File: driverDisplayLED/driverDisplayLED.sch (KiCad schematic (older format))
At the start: 16 parts

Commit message: set: 74HC245D - CONN2X8 - 74HC245D - 74HC138D
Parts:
- added C?: C, symbol Device:C
- Q? (x2): symbol FDS4953:FDS4953 -> driverDisplayLED-rescue:FDS4953-FDS4953
- U?: symbol 74HC138D:74HC138D -> driverDisplayLED-rescue:74HC138D-74HC138D
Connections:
- net labels added: A6-A7, A7-B4, B0-b5, B1-a5, B2-b6, B3-a6, B4-E3, B4-b7, B5-E2, B5B6B7-b8, B6-B6, B7-B7, GND, VCC, a4-A5
- net labels removed: a4
- wire segments 14 -> 71
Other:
- moved on the sheet: U?

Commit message: primer bloque 74HC595D: shift-register
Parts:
- added C? (x3): C, symbol Device:C
- added J? (x2): Conn_01x12_Male, symbol Connector:Conn_01x12_Male
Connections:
- net labels added: A1-SER, A5-SRCLK, G1, G2, G3, G4, G5, G6, G7, G8, H5, H6, H7, H8, R1, R2, R3, R4, R5, R6, R7, R8, RCLK, SRCLK, bus.R8-R1
- wire segments 71 -> 129
- no-connect marks 0 -> 3
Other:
- moved on the sheet: C?, U?, U?A, U?B, U?C, U?D, U?E, U?F, U?G

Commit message: segundo bloque 74HC595D: shift-register
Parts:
- removed U?: 74HC595, symbol 74xx:74HC595
- added C? (x2): C, symbol Device:C
- added J? (x2): Conn_01x12_Male, symbol Connector:Conn_01x12_Male
- added U? (x2): 74HC595, symbol 74xx:74HC595
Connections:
- net labels added: QH-SER
- wire segments 129 -> 209

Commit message: bloque inverters, bloque mosfets. Pendiente: añadir segunda hoja a derecha, conectar matrices, completar 74HC245D(1), revisar los NC.
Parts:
- removed Q? (x2): FDS4953, SOIC127P600X175-8N, symbol driverDisplayLED-rescue:FDS4953-FDS4953
- removed U?: 74HC595, symbol 74xx:74HC595
- added C? (x3): C, symbol Device:C
- added D? (x2): D, symbol Device:D
- added J? (x4): Conn_01x12_Male, symbol Connector:Conn_01x12_Male
- added Q1, Q2, Q? (x6): FDS4953-FDS4953, SOIC127P600X175-8N, symbol driverDisplayLED-rescue:FDS4953-FDS4953
- added R? (x3): R, symbol Device:R
- added RN?: R_Network04, Resistor_THT:R_Array_SIP5, symbol Device:R_Network04
- added U?: 74HC595, symbol 74xx:74HC595
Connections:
- net labels added: 1, 2, 3, 4, 5, 6, 7, 8, Y0-G2, Y1-G1, Y2-G2, Y3-G1, bus.Y4-Y7
- wire segments 209 -> 402
- no-connect marks 3 -> 7
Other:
- moved on the sheet: C?, J?, U?, U?A, U?B, U?C, U?D, U?E, U?F, U?G

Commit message: netlist, asociación de componentes
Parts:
- C1, C2, C3, C4, C5, C6, C7, C8, C9: renamed from C?; footprint (none) -> Capacitor_SMD:CP_Elec_3x5.3
- D1, D2: renamed from D?; footprint (none) -> Diode_SMD:D_0201_0603Metric
- J1, J2, J3, J5, J6, J7, J8, J9: renamed from J?; footprint (none) -> Connector_PinHeader_1.00mm:PinHeader_1x12_P1.00mm_Vertical
- J4: renamed from J?; footprint (none) -> Connector_IDC:IDC-Header_2x08_P2.54mm_Vertical
- Q1, Q2: footprint SOIC127P600X175-8N -> FDS4953:SOIC127P600X175-8N
- Q1, Q2, Q3, Q4: renamed from Q?; footprint SOIC127P600X175-8N -> FDS4953:SOIC127P600X175-8N
- R1, R2, R3: renamed from R?; footprint (none) -> Resistor_SMD:R_0201_0603Metric
- RN1: renamed from RN?; footprint Resistor_THT:R_Array_SIP5 -> Resistor_THT:R_Array_SIP4
- U1, U4: renamed from U?; footprint (none) -> Package_SO:HSOP-20-1EP_11.0x15.9mm_P1.27mm_SlugDown_ThermalVias
- U2, U3, U7, U8: renamed from U?; footprint (none) -> Package_SO:HTSSOP-16-1EP_4.4x5mm_P0.65mm_EP3.4x5mm
- U5: renamed from U?; footprint SOIC127P600X175-16N -> Package_SO:TSSOP-16_4.4x5mm_P0.65mm
- U6: renamed from U?; footprint (none) -> Package_SO:TSSOP-14_4.4x5mm_P0.65mm
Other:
- moved on the sheet: C1, C3, C5, C6, C7, C8, C9, D1, D2, J3, J7, J8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

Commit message: cambio conector 2x08 J4
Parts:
- removed J4: Conn_02x08_Row_Letter_First, Connector_IDC:IDC-Header_2x08_P2.54mm_Vertical, symbol Connector_Generic:Conn_02x08_Row_Letter_First
- added J4: Conn_02x08_Counter_Clockwise, Connector_PinHeader_2.54mm:PinHeader_2x08_P2.54mm_Vertical, symbol Connector_Generic:Conn_02x08_Counter_Clockwise
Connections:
- wire segments 402 -> 399
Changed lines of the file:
@@
 	-6650 5550 -6550 5650
-$Comp
-L Connector_Generic:Conn_02x08_Row_Letter_First J4
-U 1 1 5F69521F
-P 3750 8150
-F 0 "J4" H 3800 8667 50  0000 C CNN
-F 1 "Conn_02x08_Row_Letter_First" H 3800 8576 50  0000 C CNN
-F 2 "Connector_IDC:IDC-Header_2x08_P2.54mm_Vertical" H 3750 8150 50  0001 C CNN
-F 3 "~" H 3750 8150 50  0001 C CNN
-	1    3750 8150
-	1    0    0    -1
-$EndComp
 $Comp
 L Device:C C3
@@
 Text Label 3100 7800 2    50   ~ 0
 B2-b6
-Wire Wire Line
-	3700 8350 3650 8350
 Text Label 3100 7900 2    50   ~ 0
 B3-a6
@@
 Text Label 4050 8900 2    50   ~ 0
 B2-b6
-Wire Wire Line
-	3650 8150 3700 8150
-Wire Wire Line
-	3650 8250 3700 8250
 Wire Wire Line
 	5850 8450 6000 8450
@@
 Wire Wire Line
 	700  1300 700  8100
+$Comp
+L Connector_Generic:Conn_02x08_Counter_Clockwise J4
+U 1 1 5F72EC68
+P 3750 8150
+F 0 "J4" H 3800 8667 50  0000 C CNN
+F 1 "Conn_02x08_Counter_Clockwise" H 3800 8576 50  0000 C CNN
+F 2 "Connector_PinHeader_2.54mm:PinHeader_2x08_P2.54mm_Vertical" H 3750 8150 50  0001 C CNN
+F 3 "~" H 3750 8150 50  0001 C CNN
+	1    3750 8150
+	1    0    0    -1
+$EndComp
 $EndSCHEMATC

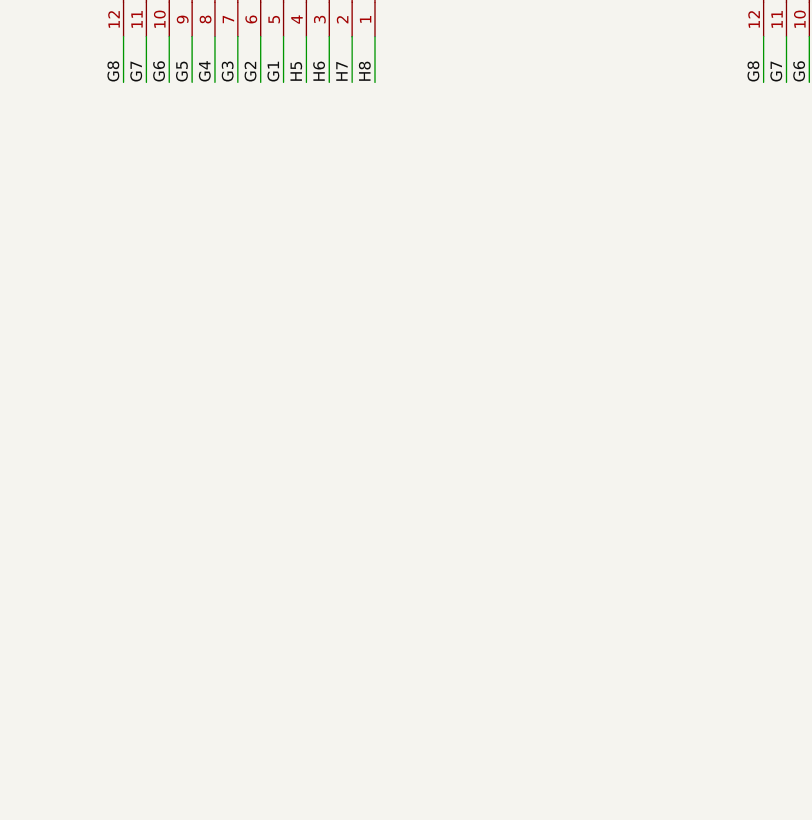
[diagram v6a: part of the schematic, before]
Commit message: agrego modulo myLedMatrix. Probar instanciar debido al path local
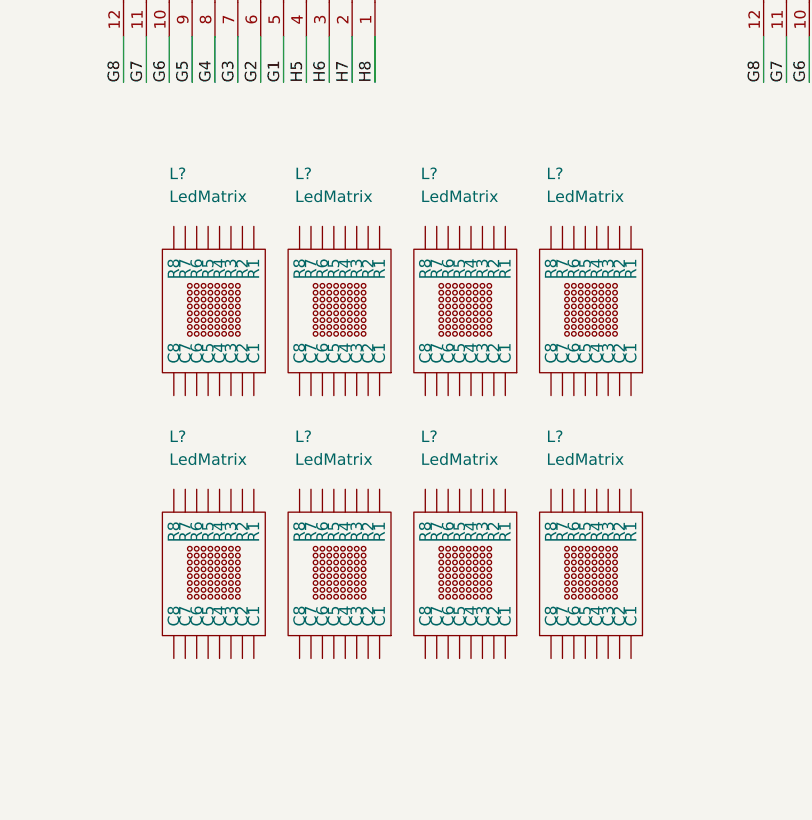
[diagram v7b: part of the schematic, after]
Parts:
- added L? (x8): LedMatrix, symbol myLedMatrix:LedMatrix
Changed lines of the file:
@@
 	1    0    0    -1
 $EndComp
+$Comp
+L myLedMatrix:LedMatrix L?
+U 1 1 5F7B4D9C
+P 1950 4550
+F 0 "L?" H 2150 3950 50  0000 R CNN
+F 1 "LedMatrix" H 2150 4050 50  0000 R CNN
+F 2 "" H 1930 4530 50  0001 C CNN
+F 3 "" H 1930 4530 50  0001 C CNN
+	1    1950 4550
+	-1   0    0    1
+$EndComp
+$Comp
+L myLedMatrix:LedMatrix L?
+U 1 1 5F7C4F20
+P 2500 4550
+F 0 "L?" H 2700 3950 50  0000 R CNN
+F 1 "LedMatrix" H 2700 4050 50  0000 R CNN
+F 2 "" H 2480 4530 50  0001 C CNN
+F 3 "" H 2480 4530 50  0001 C CNN
+	1    2500 4550
+	-1   0    0    1
+$EndComp
+$Comp
+L myLedMatrix:LedMatrix L?
+U 1 1 5F7C5FCF
+P 3050 4550
+F 0 "L?" H 3250 3950 50  0000 R CNN
+F 1 "LedMatrix" H 3250 4050 50  0000 R CNN
+F 2 "" H 3030 4530 50  0001 C CNN
+F 3 "" H 3030 4530 50  0001 C CNN
+	1    3050 4550
+	-1   0    0    1
+$EndComp
+$Comp
+L myLedMatrix:LedMatrix L?
+U 1 1 5F7C71EE
+P 3600 4550
+F 0 "L?" H 3800 3950 50  0000 R CNN
+F 1 "LedMatrix" H 3800 4050 50  0000 R CNN
+F 2 "" H 3580 4530 50  0001 C CNN
+F 3 "" H 3580 4530 50  0001 C CNN
+	1    3600 4550
+	-1   0    0    1
+$EndComp
+$Comp
+L myLedMatrix:LedMatrix L?
+U 1 1 5F7CAD02
+P 1950 5700
+F 0 "L?" H 2150 5100 50  0000 R CNN
+F 1 "LedMatrix" H 2150 5200 50  0000 R CNN
+F 2 "" H 1930 5680 50  0001 C CNN
+F 3 "" H 1930 5680 50  0001 C CNN
+	1    1950 5700
+	-1   0    0    1
+$EndComp
+$Comp
+L myLedMatrix:LedMatrix L?
+U 1 1 5F7D1CEF
+P 2500 5700
+F 0 "L?" H 2700 5100 50  0000 R CNN
+F 1 "LedMatrix" H 2700 5200 50  0000 R CNN
+F 2 "" H 2480 5680 50  0001 C CNN
+F 3 "" H 2480 5680 50  0001 C CNN
+	1    2500 5700
+	-1   0    0    1
+$EndComp
+$Comp
+L myLedMatrix:LedMatrix L?
+U 1 1 5F7D3AB8
+P 3050 5700
+F 0 "L?" H 3250 5100 50  0000 R CNN
+F 1 "LedMatrix" H 3250 5200 50  0000 R CNN
+F 2 "" H 3030 5680 50  0001 C CNN
+F 3 "" H 3030 5680 50  0001 C CNN
+	1    3050 5700
+	-1   0    0    1
+$EndComp
+$Comp
+L myLedMatrix:LedMatrix L?
+U 1 1 5F7D4FD9
+P 3600 5700
+F 0 "L?" H 3800 5100 50  0000 R CNN
+F 1 "LedMatrix" H 3800 5200 50  0000 R CNN
+F 2 "" H 3580 5680 50  0001 C CNN
+F 3 "" H 3580 5680 50  0001 C CNN
+	1    3600 5700
+	-1   0    0    1
+$EndComp
 $EndSCHEMATC

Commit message: new LedMatrix_M + array 4953 update + G1-G8 paralelo
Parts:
- removed L? (x8): LedMatrix, symbol myLedMatrix:LedMatrix
- removed Q1, Q2, Q3, Q4: FDS4953-FDS4953, FDS4953:SOIC127P600X175-8N, symbol driverDisplayLED-rescue:FDS4953-FDS4953
- added L1, L2, L? (x2): LedMatrix_M, symbol myLedMatrix:LedMatrix_M
- added Q? (x8): FDS4953, SOIC127P600X175-8N, symbol driverDisplayLED-rescue:FDS4953-FDS4953
- added RN?: R_Network04, Resistor_THT:R_Array_SIP4, symbol Device:R_Network04
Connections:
- net labels added: D1-H2, D1-H4, D2-H1, D2-H3, Y4-G2, Y5-G1, Y6-G2, Y7-G1
- net labels removed: 1, 2, 3, 4, 5, 6, 7, 8, bus.Y4-Y7
- wire segments 399 -> 393
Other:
- moved on the sheet: C1, C2, C3, C4, C5, C6, C7, C8, C9, D1, D2, J1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
